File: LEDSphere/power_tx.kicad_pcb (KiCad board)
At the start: 2 copper layers, 124 x 120 mm, 91 parts, among them J1 USB_C_Receptacle_USB2.0, M1 Motor_DC, Q1 BSS138, Q2 BSS138, Q3 BSS138, Q4 BSS138, Q5 BSS138, Q6 BSS138, Q7 Si2319CDS, Q8 Si2319CDS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

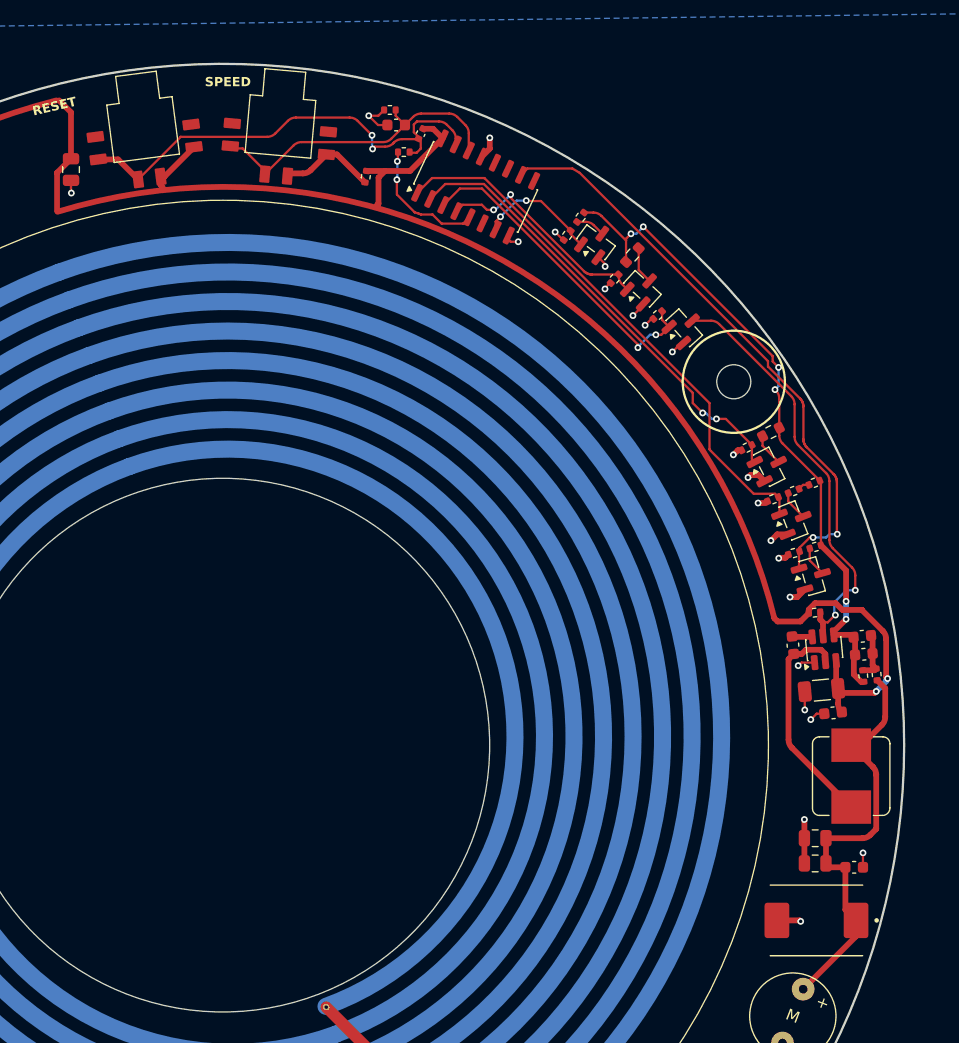
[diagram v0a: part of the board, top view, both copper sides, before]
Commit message: Altered Button Part
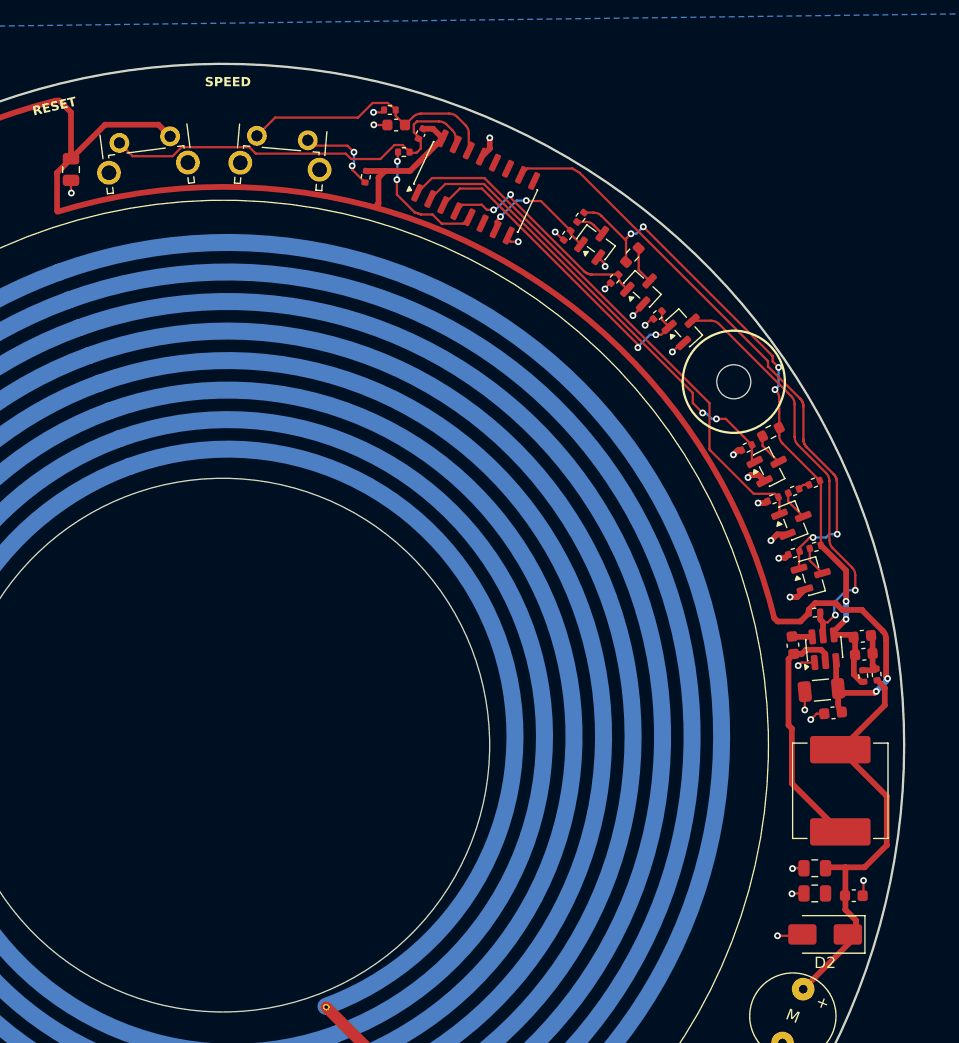
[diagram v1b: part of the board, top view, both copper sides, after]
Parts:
- D2: footprint Footprints:DIOM7959X262N -> Diode_SMD:D_SMA
- L1: footprint Inductor_SMD:L_Bourns_SRP7028A_7.3x6.6mm -> Inductor_SMD:L_Vishay_IHLP-3232
- SW1, SW2: value ~ -> SW_Push; footprint Footprints:XKB5858-X-F-75 -> Button_Switch_THT:SW_Tactile_SPST_Angled_PTS645Vx58-2LFS
- moved C12 2.64 mm to (188.4, 107.0)
- moved C14 2.64 mm to (188.4, 109.2)
- moved C17 2.50 mm to (191.8, 109.4)
- moved SW2 2.39 mm to (127.2, 43.1)
- moved SW1 2.23 mm to (139.3, 42.5)
- moved L1 1.61 mm to (190.7, 100.2)
- moved D2 1.45 mm to (189.3, 112.8)
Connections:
- SW1 pad 1: unconnected-(SW1-Pad1) -> Net-(U1-CLK)
- SW1 pad 2: Net-(U1-CLK) -> Net-(R1-Pad2)
- SW2 pad 1: unconnected-(SW2-Pad1) -> Net-(U1-Reset)
- SW2 pad 2: Net-(U1-Reset) -> +12V
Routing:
- net Net-(U1-Reset): track 42.0 -> 36.2 mm, vias 2 -> 0
- net +12V: track 158.9 -> 164.3 mm
- net Net-(U1-CLK): track 28.2 -> 23.7 mm
- net GND: track 113.2 -> 110.0 mm, vias 51 -> 53
- net Net-(U3-SW): track 19.7 -> 21.5 mm
- net Net-(R1-Pad2): track 8.24 -> 7.50 mm, vias 0 -> 2

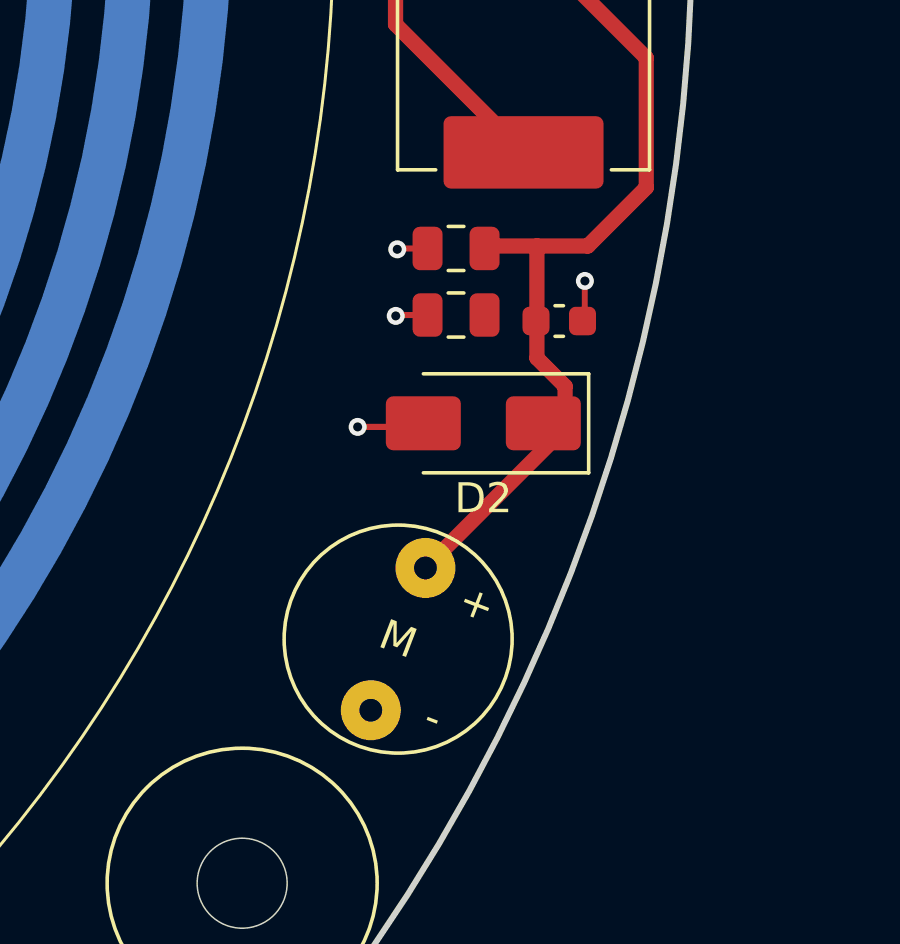
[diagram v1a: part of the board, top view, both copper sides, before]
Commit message: Edit 22uF Footprint to 1210
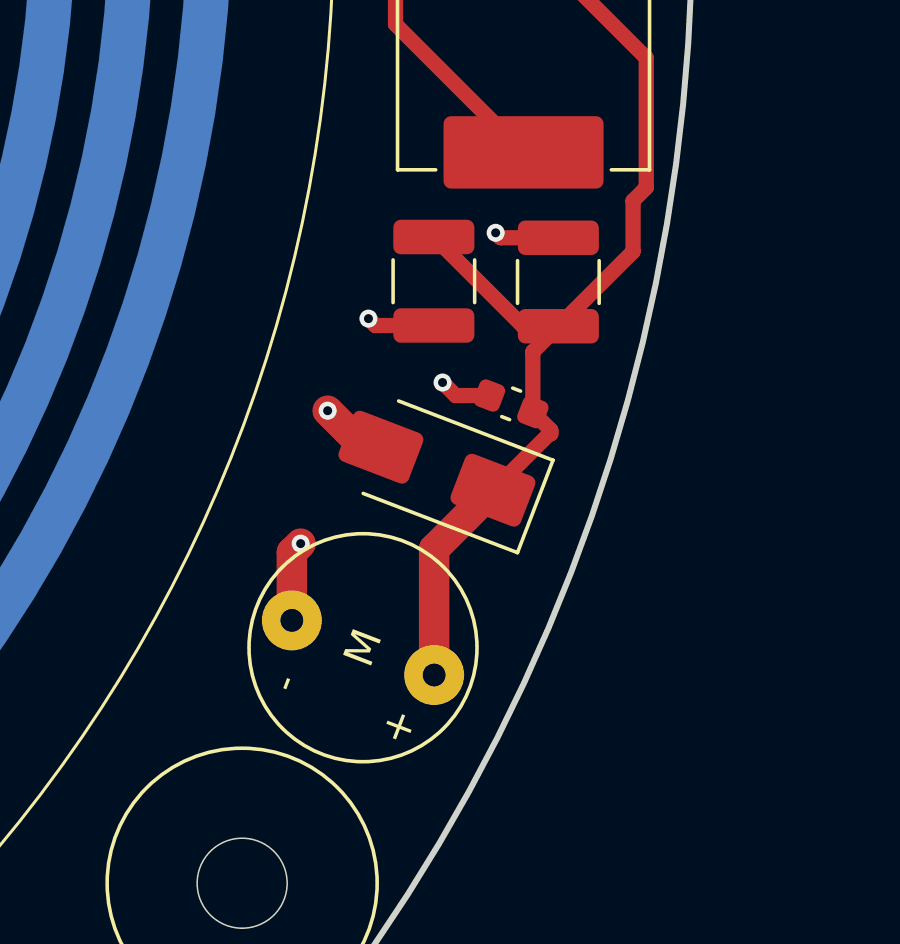
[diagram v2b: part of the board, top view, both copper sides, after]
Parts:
- C12, C14: footprint Capacitor_SMD:C_0805_2012Metric -> Capacitor_SMD:C_1210_3225Metric
- moved M1 7.07 mm to (190.1, 122.1), turned to -111 degrees
- moved C14 3.58 mm to (191.8, 108.1), turned to 90 degrees
- moved C17 3.19 mm to (190.2, 112.2), turned to 159 degrees
- moved D2 2.16 mm to (187.8, 114.3), turned to 159 degrees
- moved C12 1.32 mm to (187.7, 108.1), turned to -90 degrees
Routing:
- net Motor: track 37.5 -> 43.2 mm
- net GND: track 110.0 -> 115.4 mm, vias 53 -> 54

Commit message: Edit testpoint footprint
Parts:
- TP1, TP2, TP3: footprint TestPoint:TestPoint_Loop_D1.80mm_Drill1.0mm_Beaded -> TestPoint:TestPoint_THTPad_D2.0mm_Drill1.0mm

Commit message: Most up to date TX
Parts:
- added TP4: TestPoint, TestPoint:TestPoint_Pad_1.0x1.0mm, F.Cu at (160.3, 140.7)
- added TP5: TestPoint, TestPoint:TestPoint_Pad_1.0x1.0mm, F.Cu at (162.6, 139.3)
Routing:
- net Net-(C26-Pad2): track 13.8 -> 16.7 mm
- net GND: track 115.4 -> 117.3 mm
